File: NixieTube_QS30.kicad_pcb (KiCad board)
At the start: 2 copper layers, 37 x 56.3 mm, 67 parts, among them J1 Conn_01x06_Male, J2 HV_IN, J3 Conn_01x06_Female, J4 HV_OUT, Q1 MMBTA42LT1, Q10 MMBTA42LT1, Q11 AO3400, Q12 AO3400, Q13 AO3400, Q14 MMBTA42LT1, Q15 MMBTA42LT1, Q2 MMBTA42LT1, Q3 MMBTA42LT1, Q4 MMBTA42LT1, Q5 MMBTA42LT1, Q6 MMBTA42LT1, Q7 MMBTA42LT1, Q8 MMBTA42LT1, Q9 MMBTA42LT1, U1 74HC595D, U2 nixie-tube, U3 74HC595D, U4 ams1117-5.0

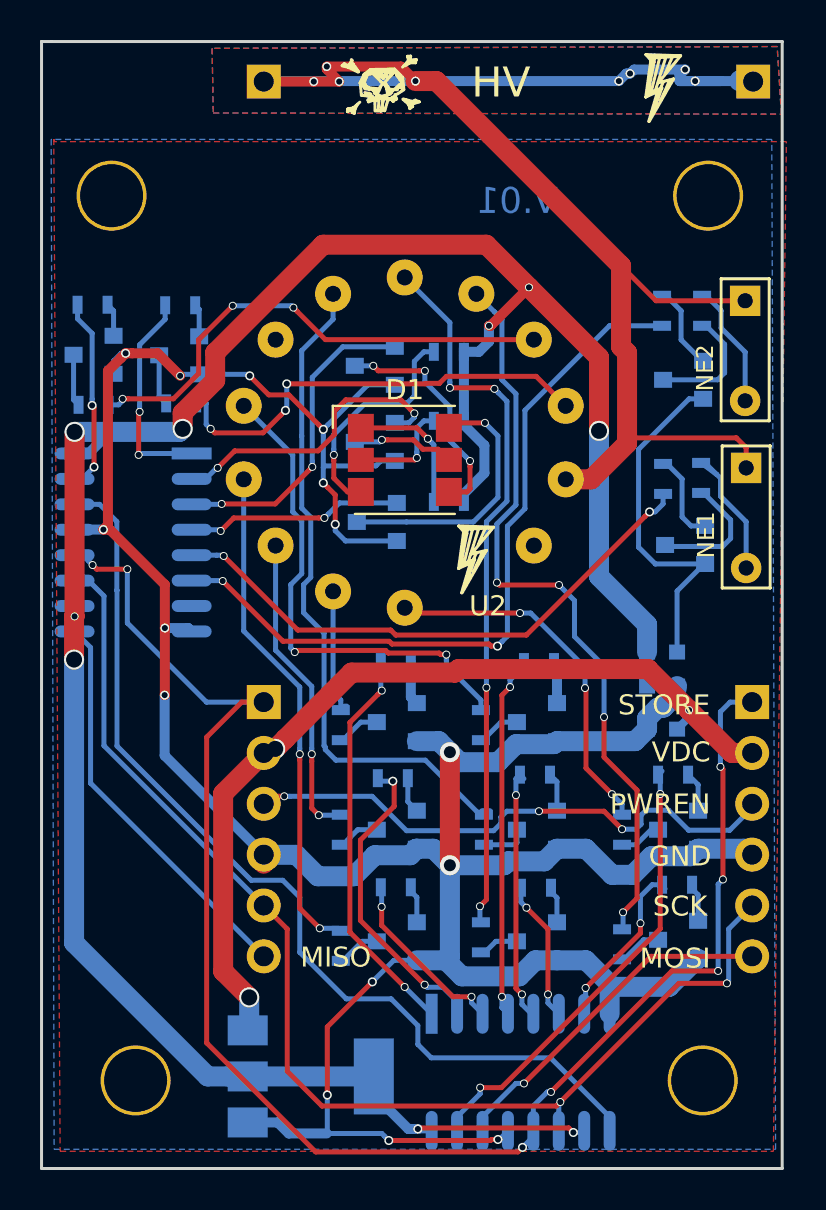
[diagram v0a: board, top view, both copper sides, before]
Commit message: checked all components, adjusted tracks
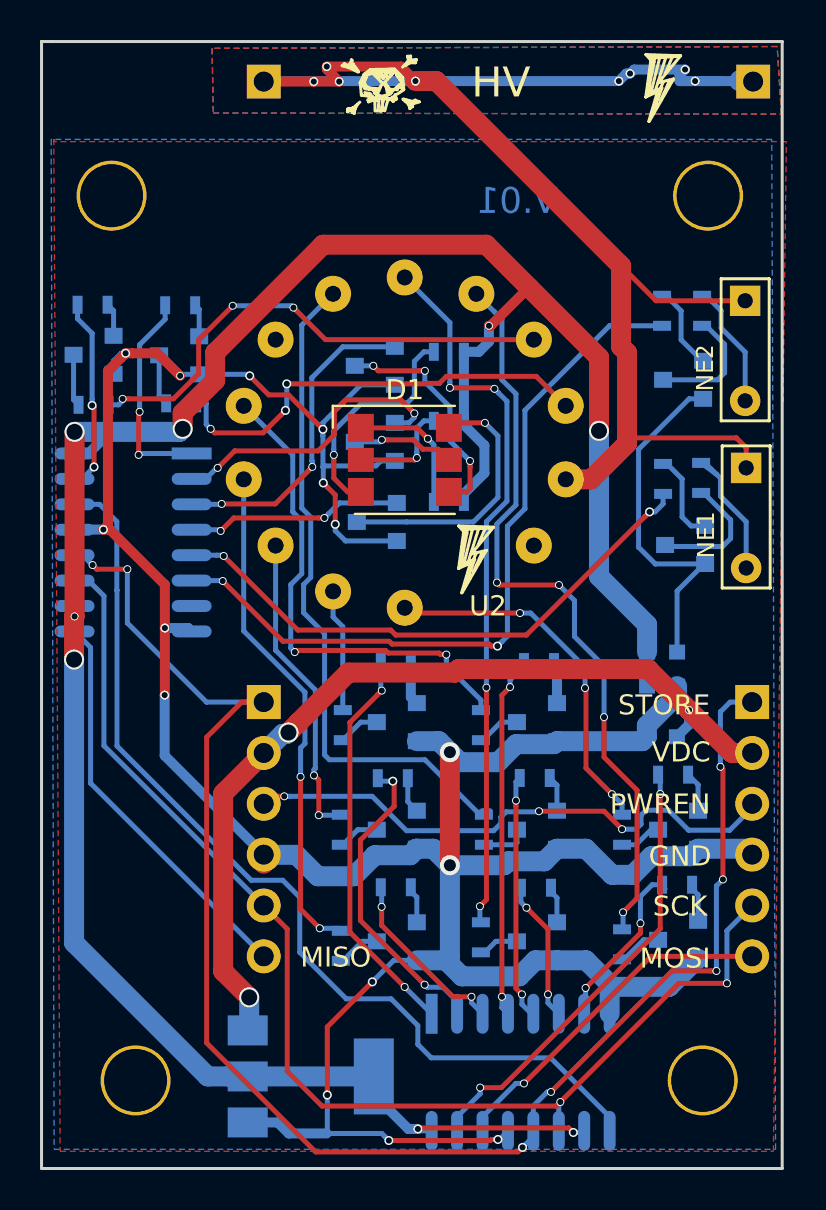
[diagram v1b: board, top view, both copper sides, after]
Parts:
- moved C1 0.38 mm to (182.5, 75.0)
- moved R23 0.17 mm to (176.1, 77.1)
- moved R9 0.10 mm to (166.6, 74.5)
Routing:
- net +5V: track 125.6 -> 125.4 mm, vias 9 -> 8
